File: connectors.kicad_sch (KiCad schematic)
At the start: 6 parts

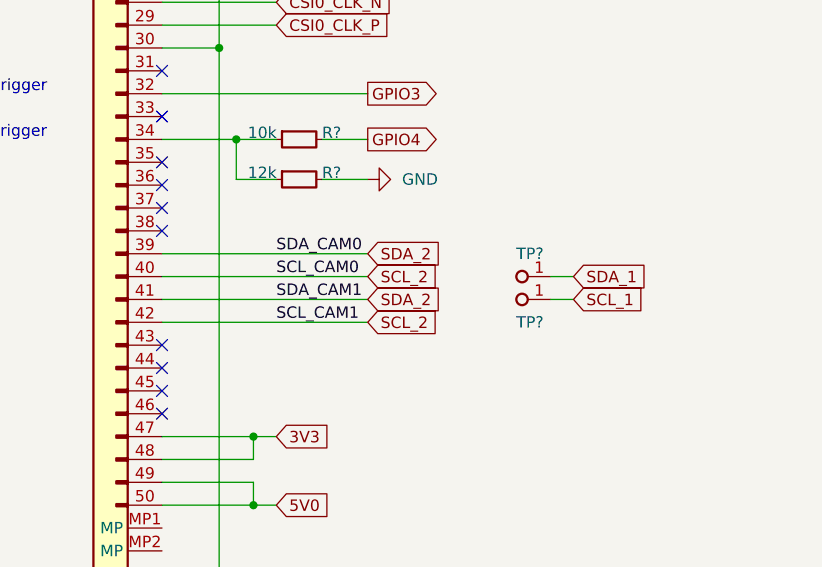
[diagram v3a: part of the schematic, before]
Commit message: Add resistor selectable i2c
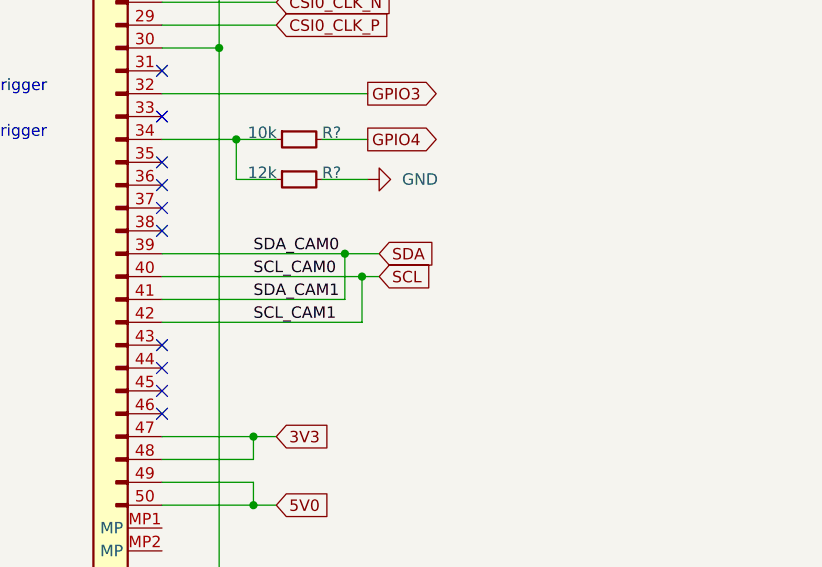
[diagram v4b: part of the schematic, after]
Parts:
- removed TP? (x2): TP_1.5mm_SMD, antmicro-footprints:TP_SMD_1.5mm, symbol antmicroTestPoints:TP_1.5mm_SMD
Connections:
- net SCL_2 renamed SCL
- net SDA_2 renamed SDA
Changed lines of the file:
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@@
   (junction (at 137.16 151.13) (diameter 0) (color 0 0 0 0)
+  )
+  (junction (at 149.225 133.35) (diameter 0) (color 0 0 0 0)
+  )
+  (junction (at 147.32 130.81) (diameter 0) (color 0 0 0 0)
   )
   (junction (at 133.35 77.47) (diameter 0) (color 0 0 0 0)
@@
     (stroke (width 0) (type default) (color 0 0 0 0))
   )
-  (wire (pts (xy 127 138.43) (xy 149.86 138.43))
-    (stroke (width 0) (type default) (color 0 0 0 0))
-  )
   (wire (pts (xy 133.35 100.33) (xy 127 100.33))
     (stroke (width 0) (type default) (color 0 0 0 0))
   )
-  (wire (pts (xy 170.18 135.89) (xy 172.72 135.89))
+  (wire (pts (xy 147.32 130.81) (xy 151.13 130.81))
     (stroke (width 0) (type default) (color 0 0 0 0))
   )
@@
     (stroke (width 0) (type default) (color 0 0 0 0))
   )
+  (wire (pts (xy 147.32 130.81) (xy 147.32 135.89))
+    (stroke (width 0) (type default) (color 0 0 0 0))
+  )
+  (wire (pts (xy 149.225 133.35) (xy 151.13 133.35))
+    (stroke (width 0) (type default) (color 0 0 0 0))
+  )
+  (wire (pts (xy 127 130.81) (xy 147.32 130.81))
+    (stroke (width 0) (type default) (color 0 0 0 0))
+  )
   (wire (pts (xy 127 87.63) (xy 139.7 87.63))
     (stroke (width 0) (type default) (color 0 0 0 0))
   )
-  (wire (pts (xy 170.18 133.35) (xy 172.72 133.35))
+  (wire (pts (xy 127 133.35) (xy 149.225 133.35))
     (stroke (width 0) (type default) (color 0 0 0 0))
   )
@@
     (stroke (width 0) (type default) (color 0 0 0 0))
   )
-  (wire (pts (xy 127 130.81) (xy 149.86 130.81))
-    (stroke (width 0) (type default) (color 0 0 0 0))
-  )
   (wire (pts (xy 127 97.79) (xy 139.7 97.79))
     (stroke (width 0) (type default) (color 0 0 0 0))
   )
+  (wire (pts (xy 149.225 138.43) (xy 149.225 133.35))
+    (stroke (width 0) (type default) (color 0 0 0 0))
+  )
   (wire (pts (xy 127 80.01) (xy 139.7 80.01))
     (stroke (width 0) (type default) (color 0 0 0 0))
@@
     (stroke (width 0) (type default) (color 0 0 0 0))
   )
+  (wire (pts (xy 127 135.89) (xy 147.32 135.89))
+    (stroke (width 0) (type default) (color 0 0 0 0))
+  )
   (wire (pts (xy 133.35 62.23) (xy 133.35 69.85))
     (stroke (width 0) (type default) (color 0 0 0 0))
@@
     (stroke (width 0) (type default) (color 0 0 0 0))
   )
-  (wire (pts (xy 127 133.35) (xy 149.86 133.35))
-    (stroke (width 0) (type default) (color 0 0 0 0))
-  )
   (wire (pts (xy 127 82.55) (xy 139.7 82.55))
     (stroke (width 0) (type default) (color 0 0 0 0))
@@
     (stroke (width 0) (type default) (color 0 0 0 0))
   )
+  (wire (pts (xy 127 138.43) (xy 149.225 138.43))
+    (stroke (width 0) (type default) (color 0 0 0 0))
+  )
   (wire (pts (xy 127 156.21) (xy 137.16 156.21))
     (stroke (width 0) (type default) (color 0 0 0 0))
   )
   (wire (pts (xy 127 113.03) (xy 149.86 113.03))
-    (stroke (width 0) (type default) (color 0 0 0 0))
-  )
-  (wire (pts (xy 127 135.89) (xy 149.86 135.89))
     (stroke (width 0) (type default) (color 0 0 0 0))
   )
@@
     (effects (font (size 1.27 1.27) (thickness 0.254) bold) (justify left bottom))
   )
-  (label "SDA_CAM1" (at 139.7 135.89 0)
+  (label "SDA_CAM1" (at 137.16 135.89 0)
     (effects (font (size 1.27 1.27)) (justify left bottom))
   )
-  (label "SCL_CAM1" (at 139.7 138.43 0)
+  (label "SCL_CAM1" (at 137.16 138.43 0)
     (effects (font (size 1.27 1.27)) (justify left bottom))
   )
-  (label "SDA_CAM0" (at 139.7 130.81 0)
+  (label "SDA_CAM0" (at 137.16 130.81 0)
     (effects (font (size 1.27 1.27)) (justify left bottom))
   )
-  (label "SCL_CAM0" (at 139.7 133.35 0)
+  (label "SCL_CAM0" (at 137.16 133.35 0)
     (effects (font (size 1.27 1.27)) (justify left bottom))
   )
@@
     )
   )
-  (global_label "SDA_1" (shape input) (at 172.72 133.35 0) (fields_autoplaced)
-    (effects (font (size 1.27 1.27)) (justify left))
-    (property "Intersheet References" "${INTERSHEET_REFS}" (id 0) (at 180.8783 133.2706 0)
-      (effects (font (size 1.27 1.27)) (justify left) hide)
-    )
-  )
-  (global_label "SCL_2" (shape input) (at 149.86 138.43 0) (fields_autoplaced)
-    (effects (font (size 1.27 1.27)) (justify left))
-    (property "Intersheet References" "${INTERSHEET_REFS}" (id 0) (at 157.9579 138.3506 0)
-      (effects (font (size 1.27 1.27)) (justify left) hide)
-    )
-  )
-  (global_label "SCL_2" (shape input) (at 149.86 133.35 0) (fields_autoplaced)
-    (effects (font (size 1.27 1.27)) (justify left))
-    (property "Intersheet References" "${INTERSHEET_REFS}" (id 0) (at 157.9579 133.2706 0)
-      (effects (font (size 1.27 1.27)) (justify left) hide)
-    )
-  )
   (global_label "GPIO3" (shape output) (at 149.86 113.03 0) (fields_autoplaced)
     (effects (font (size 1.27 1.27)) (justify left))
@@
     )
   )
-  (global_label "SDA_2" (shape input) (at 149.86 135.89 0) (fields_autoplaced)
-    (effects (font (size 1.27 1.27)) (justify left))
-    (property "Intersheet References" "${INTERSHEET_REFS}" (id 0) (at 158.0183 135.8106 0)
-      (effects (font (size 1.27 1.27)) (justify left) hide)
-    )
-  )
   (global_label "CSI0_D1_N" (shape output) (at 139.7 90.17 0) (fields_autoplaced)
     (effects (font (size 1.27 1.27)) (justify left))
@@
     )
   )
-  (global_label "SDA_2" (shape input) (at 149.86 130.81 0) (fields_autoplaced)
-    (effects (font (size 1.27 1.27)) (justify left))
-    (property "Intersheet References" "${INTERSHEET_REFS}" (id 0) (at 158.0183 130.7306 0)
-      (effects (font (size 1.27 1.27)) (justify left) hide)
-    )
-  )
   (global_label "CSI1_D1_P" (shape output) (at 139.7 82.55 0) (fields_autoplaced)
     (effects (font (size 1.27 1.27)) (justify left))
@@
     )
   )
-  (global_label "SCL_1" (shape input) (at 172.72 135.89 0) (fields_autoplaced)
+  (global_label "SDA" (shape input) (at 151.13 130.81 0) (fields_autoplaced)
     (effects (font (size 1.27 1.27)) (justify left))
-    (property "Intersheet References" "${INTERSHEET_REFS}" (id 0) (at 180.8179 135.8106 0)
+    (property "Intersheet References" "${INTERSHEET_REFS}" (id 0) (at 157.1112 130.7306 0)
       (effects (font (size 1.27 1.27)) (justify left) hide)
     )
   )
-  (symbol (lib_id "antmicroTestPoints:TP_1.5mm_SMD") (at 170.18 133.35 180) (unit 1)
-    (in_bom yes) (on_board yes)
-    (property "Reference" "TP?" (id 0) (at 166.37 130.81 0)
-      (effects (font (size 1.27 1.27) (thickness 0.15)) (justify right))
+  (global_label "SCL" (shape input) (at 151.13 133.35 0) (fields_autoplaced)
+    (effects (font (size 1.27 1.27)) (justify left))
+    (property "Intersheet References" "${INTERSHEET_REFS}" (id 0) (at 157.0507 133.2706 0)
+      (effects (font (size 1.27 1.27)) (justify left) hide)
     )
-    (property "Value" "TP_1.5mm_SMD" (id 1) (at 154.94 125.73 0)
-      (effects (font (size 1.27 1.27) (thickness 0.15)) (justify left bottom) hide)
-    )
-    (property "Footprint" "antmicro-footprints:TP_SMD_1.5mm" (id 2) (at 154.94 123.19 0)
-      (effects (font (size 1.27 1.27) (thickness 0.15)) (justify left bottom) hide)
-    )
-    (property "Datasheet" "" (id 3) (at 152.4 120.65 0)
-      (effects (font (size 1.27 1.27) (thickness 0.15)) (justify left bottom) hide)
-    )
-    (property "MPN" "" (id 4) (at 170.18 133.35 0)
-      (effects (font (size 1.27 1.27)) hide)
-    )
-    (property "Manufacturer" "" (id 5) (at 170.18 133.35 0)
-      (effects (font (size 1.27 1.27)) hide)
-    )
-    (property "Author" "Antmicro" (id 6) (at 154.94 118.11 0)
-      (effects (font (size 1.27 1.27) (thickness 0.15)) (justify left bottom) hide)
-    )
-    (property "License" "Apache-2.0" (id 7) (at 154.94 115.57 0)
-      (effects (font (size 1.27 1.27) (thickness 0.15)) (justify left bottom) hide)
-    )
-    (pin "1")
-  )
-  (symbol (lib_id "antmicroTestPoints:TP_1.5mm_SMD") (at 170.18 135.89 180) (unit 1)
-    (in_bom yes) (on_board yes)
-    (property "Reference" "TP?" (id 0) (at 166.37 138.43 0)
-      (effects (font (size 1.27 1.27) (thickness 0.15)) (justify right))
-    )
-    (property "Value" "TP_1.5mm_SMD" (id 1) (at 154.94 128.27 0)
-      (effects (font (size 1.27 1.27) (thickness 0.15)) (justify left bottom) hide)
-    )
-    (property "Footprint" "antmicro-footprints:TP_SMD_1.5mm" (id 2) (at 154.94 125.73 0)
-      (effects (font (size 1.27 1.27) (thickness 0.15)) (justify left bottom) hide)
-    )
-    (property "Datasheet" "" (id 3) (at 152.4 123.19 0)
-      (effects (font (size 1.27 1.27) (thickness 0.15)) (justify left bottom) hide)
-    )
-    (property "MPN" "" (id 4) (at 170.18 135.89 0)
-      (effects (font (size 1.27 1.27)) hide)
-    )
-    (property "Manufacturer" "" (id 5) (at 170.18 135.89 0)
-      (effects (font (size 1.27 1.27)) hide)
-    )
-    (property "Author" "Antmicro" (id 6) (at 154.94 120.65 0)
-      (effects (font (size 1.27 1.27) (thickness 0.15)) (justify left bottom) hide)
-    )
-    (property "License" "Apache-2.0" (id 7) (at 154.94 118.11 0)
-      (effects (font (size 1.27 1.27) (thickness 0.15)) (justify left bottom) hide)
-    )
-    (pin "1")
   )
   (symbol (lib_id "antmicropower:GND") (at 133.35 170.18 0) (unit 1)

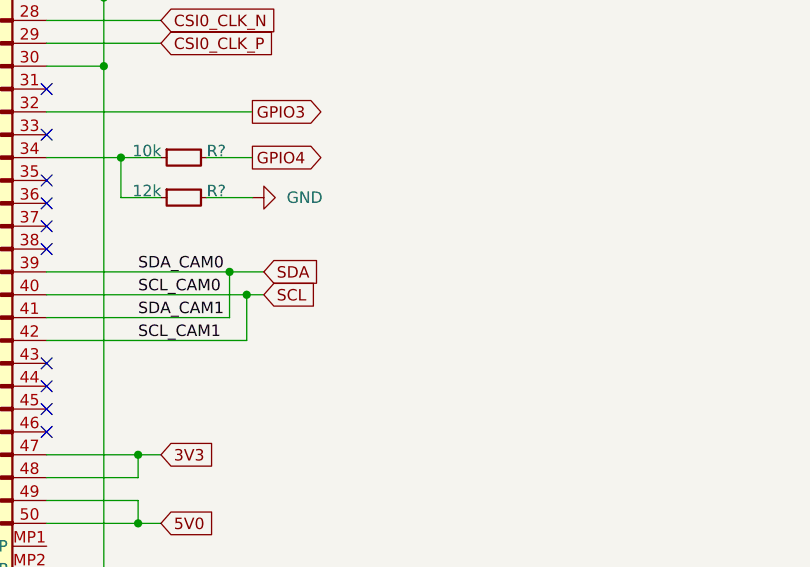
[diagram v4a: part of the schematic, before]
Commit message: Add low-capacitance TVS to serial output
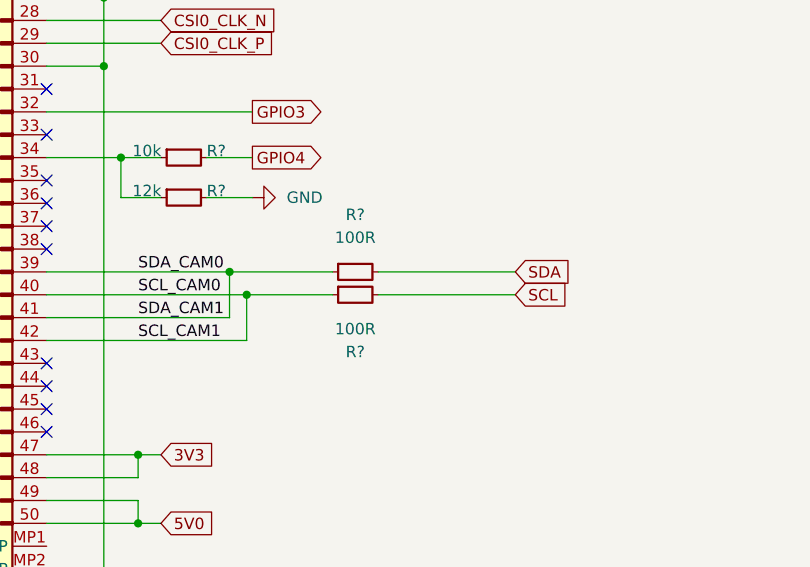
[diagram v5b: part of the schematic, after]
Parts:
- added R? (x2): R_100R_0402, antmicro-footprints:R_0402_1005Metric, symbol antmicroResistors0402:R_100R_0402
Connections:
- net SCL: now also R?.2; no longer J?.40, J?.42
- net SDA: now also R?.2; no longer J?.39, J?.41
- new net SCL_CAM0: J?.40, J?.42, R?.1
- new net SDA_CAM0: J?.39, J?.41, R?.1
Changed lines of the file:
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@@
+    (stroke (width 0) (type default) (color 0 0 0 0))
+  )
+  (wire (pts (xy 163.83 133.35) (xy 179.07 133.35))
     (stroke (width 0) (type default) (color 0 0 0 0))
   )
@@
     (stroke (width 0) (type default) (color 0 0 0 0))
   )
-  (wire (pts (xy 147.32 130.81) (xy 151.13 130.81))
-    (stroke (width 0) (type default) (color 0 0 0 0))
-  )
   (wire (pts (xy 137.16 151.13) (xy 139.7 151.13))
     (stroke (width 0) (type default) (color 0 0 0 0))
@@
     (stroke (width 0) (type default) (color 0 0 0 0))
   )
-  (wire (pts (xy 149.225 133.35) (xy 151.13 133.35))
+  (wire (pts (xy 149.225 133.35) (xy 158.75 133.35))
+    (stroke (width 0) (type default) (color 0 0 0 0))
+  )
+  (wire (pts (xy 163.83 130.81) (xy 179.07 130.81))
     (stroke (width 0) (type default) (color 0 0 0 0))
   )
@@
   )
   (wire (pts (xy 127 138.43) (xy 149.225 138.43))
+    (stroke (width 0) (type default) (color 0 0 0 0))
+  )
+  (wire (pts (xy 147.32 130.81) (xy 158.75 130.81))
     (stroke (width 0) (type default) (color 0 0 0 0))
   )
@@
     )
   )
-  (global_label "SDA" (shape input) (at 151.13 130.81 0) (fields_autoplaced)
+  (global_label "SDA" (shape input) (at 179.07 130.81 0) (fields_autoplaced)
     (effects (font (size 1.27 1.27)) (justify left))
-    (property "Intersheet References" "${INTERSHEET_REFS}" (id 0) (at 157.1112 130.7306 0)
+    (property "Intersheet References" "${INTERSHEET_REFS}" (id 0) (at 185.0512 130.7306 0)
       (effects (font (size 1.27 1.27)) (justify left) hide)
     )
   )
-  (global_label "SCL" (shape input) (at 151.13 133.35 0) (fields_autoplaced)
+  (global_label "SCL" (shape input) (at 179.07 133.35 0) (fields_autoplaced)
     (effects (font (size 1.27 1.27)) (justify left))
-    (property "Intersheet References" "${INTERSHEET_REFS}" (id 0) (at 157.0507 133.2706 0)
+    (property "Intersheet References" "${INTERSHEET_REFS}" (id 0) (at 184.9907 133.2706 0)
       (effects (font (size 1.27 1.27)) (justify left) hide)
     )
@@
     (pin "4")
     (pin "5")
+  )
+  (symbol (lib_id "antmicroResistors0402:R_100R_0402") (at 158.75 130.81 0) (unit 1)
+    (in_bom yes) (on_board yes) (fields_autoplaced)
+    (property "Reference" "R?" (id 0) (at 161.29 124.46 0)
+      (effects (font (size 1.27 1.27) (thickness 0.15)))
+    )
+    (property "Value" "R_100R_0402" (id 1) (at 179.07 143.51 0)
+      (effects (font (size 1.27 1.27) (thickness 0.15)) (justify left bottom) hide)
+    )
+    (property "Footprint" "antmicro-footprints:R_0402_1005Metric" (id 2) (at 179.07 146.05 0)
+      (effects (font (size 1.27 1.27) (thickness 0.15)) (justify left bottom) hide)
+    )
+    (property "Datasheet" "https://www.bourns.com/docs/product-datasheets/cr.pdf" (id 3) (at 179.07 148.59 0)
+      (effects (font (size 1.27 1.27) (thickness 0.15)) (justify left bottom) hide)
+    )
+    (property "MPN" "CR0402-FX-1000GLF" (id 4) (at 179.07 151.13 0)
+      (effects (font (size 1.27 1.27) (thickness 0.15)) (justify left bottom) hide)
+    )
+    (property "Manufacturer" "Bourns" (id 5) (at 179.07 153.67 0)
+      (effects (font (size 1.27 1.27) (thickness 0.15)) (justify left bottom) hide)
+    )
+    (property "License" "Apache-2.0" (id 6) (at 179.07 156.21 0)
+      (effects (font (size 1.27 1.27) (thickness 0.15)) (justify left bottom) hide)
+    )
+    (property "Author" "Antmicro" (id 7) (at 179.07 158.75 0)
+      (effects (font (size 1.27 1.27) (thickness 0.15)) (justify left bottom) hide)
+    )
+    (property "Val" "100R" (id 8) (at 161.29 127 0)
+      (effects (font (size 1.27 1.27) (thickness 0.15)))
+    )
+    (property "Tolerance" "1%" (id 9) (at 179.07 140.97 0)
+      (effects (font (size 1.27 1.27)) (justify left bottom) hide)
+    )
+    (pin "1")
+    (pin "2")
   )
   (symbol (lib_id "antmicroFCCConnectors:Conn_FFC_WE_68715014022") (at 127 34.29 0) (mirror y) (unit 1)
@@
     (pin "1")
   )
+  (symbol (lib_id "antmicroResistors0402:R_100R_0402") (at 158.75 133.35 0) (unit 1)
+    (in_bom yes) (on_board yes)
+    (property "Reference" "R?" (id 0) (at 161.29 139.7 0)
+      (effects (font (size 1.27 1.27) (thickness 0.15)))
+    )
+    (property "Value" "R_100R_0402" (id 1) (at 179.07 146.05 0)
+      (effects (font (size 1.27 1.27) (thickness 0.15)) (justify left bottom) hide)
+    )
+    (property "Footprint" "antmicro-footprints:R_0402_1005Metric" (id 2) (at 179.07 148.59 0)
+      (effects (font (size 1.27 1.27) (thickness 0.15)) (justify left bottom) hide)
+    )
+    (property "Datasheet" "https://www.bourns.com/docs/product-datasheets/cr.pdf" (id 3) (at 179.07 151.13 0)
+      (effects (font (size 1.27 1.27) (thickness 0.15)) (justify left bottom) hide)
+    )
+    (property "MPN" "CR0402-FX-1000GLF" (id 4) (at 179.07 153.67 0)
+      (effects (font (size 1.27 1.27) (thickness 0.15)) (justify left bottom) hide)
+    )
+    (property "Manufacturer" "Bourns" (id 5) (at 179.07 156.21 0)
+      (effects (font (size 1.27 1.27) (thickness 0.15)) (justify left bottom) hide)
+    )
+    (property "License" "Apache-2.0" (id 6) (at 179.07 158.75 0)
+      (effects (font (size 1.27 1.27) (thickness 0.15)) (justify left bottom) hide)
+    )
+    (property "Author" "Antmicro" (id 7) (at 179.07 161.29 0)
+      (effects (font (size 1.27 1.27) (thickness 0.15)) (justify left bottom) hide)
+    )
+    (property "Val" "100R" (id 8) (at 161.29 137.16 0)
+      (effects (font (size 1.27 1.27) (thickness 0.15)))
+    )
+    (property "Tolerance" "1%" (id 9) (at 179.07 143.51 0)
+      (effects (font (size 1.27 1.27)) (justify left bottom) hide)
+    )
+    (pin "1")
+    (pin "2")
+  )
 )

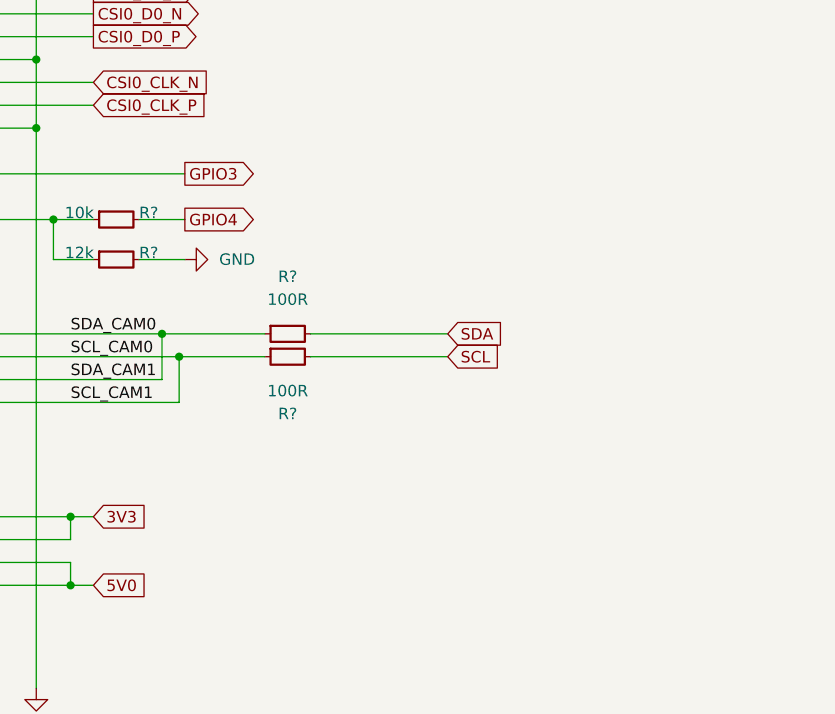
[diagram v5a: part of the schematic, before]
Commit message: Add I2C protection
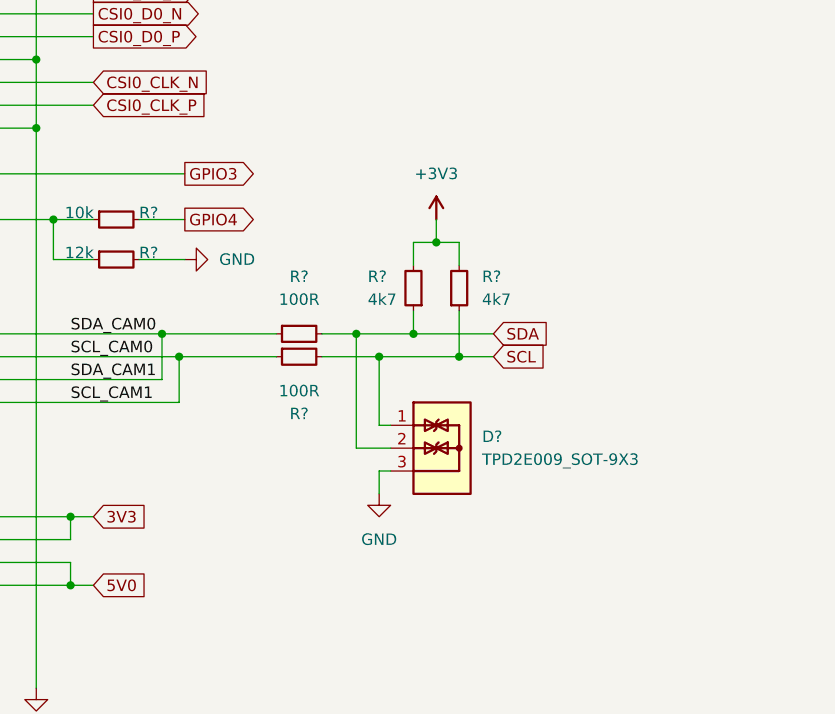
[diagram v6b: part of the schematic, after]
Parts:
- added D?: TPD2E009_SOT-9X3, antmicro-footprints:SOT-723, symbol antmicroTVSDiodes:TPD2E009_SOT-9X3
- added R? (x2): R_4k7_0402, antmicro-footprints:R_0402_1005Metric, symbol antmicroResistors0402:R_4k7_0402
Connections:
- net GND: now also D?.3
- net SCL: now also D?.1, R?.1
- net SDA: now also D?.2, R?.1
- new net +3V3: R?.2, R?.2
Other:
- moved on the sheet: R?
